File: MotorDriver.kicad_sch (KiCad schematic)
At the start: 51 parts, among them J1 Conn_01x02, J101 USB4105-GF-A, J2 Conn_01x02, J3 Conn_01x02, J4 Conn_01x02, J5 Conn_01x02, J6 Conn_01x02, U11 AS5600L-ASOM, U2 RP2040, U3 AMS1117-3.3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

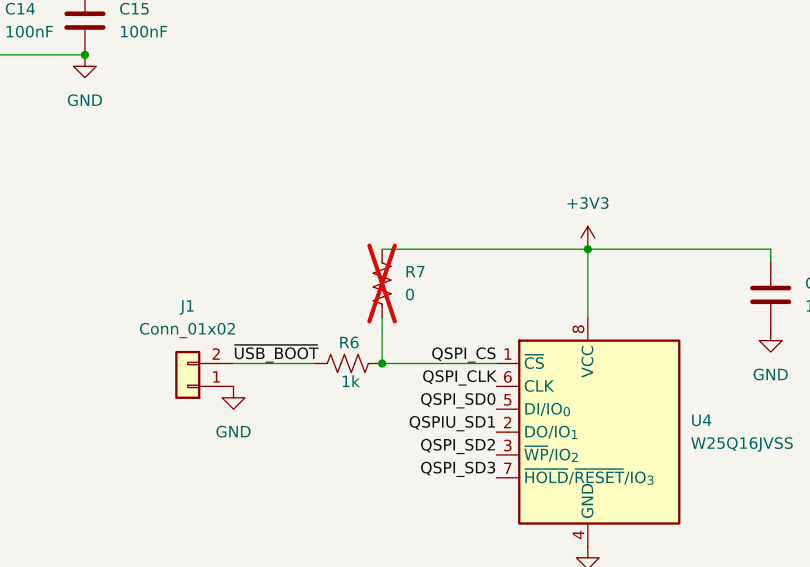
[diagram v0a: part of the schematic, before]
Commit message: populate 10k
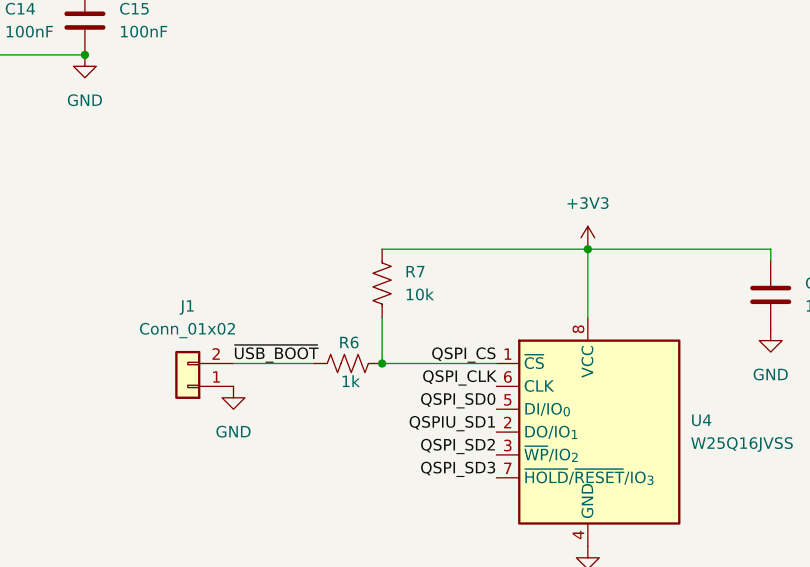
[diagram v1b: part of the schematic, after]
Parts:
- R7: value 0 -> 10k; now fitted
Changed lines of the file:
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@@
 		(in_bom yes)
 		(on_board yes)
-		(dnp yes)
+		(dnp no)
 		(fields_autoplaced yes)
 		(property "Reference" "R7"
@@
 			)
 		)
-		(property "Value" "0"
+		(property "Value" "10k"
 			(at 274.32 137.1599 0)
 			(effects
